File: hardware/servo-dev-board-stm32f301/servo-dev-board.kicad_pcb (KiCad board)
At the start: 4 copper layers, 51.5 x 26.5 mm, 39 parts, among them J1 USB_B_Micro, J2 Conn_01x05_MountingPin, J3 Conn_01x04_MountingPin, J4 Conn_01x04_MountingPin, J5 Conn_02x05_Odd_Even, SW1 SW_Push, SW2 SW_Push, U1 DRV8231ADSGR, U2 SSP7615-33DFR, U3 STM32F301K8Ux, Y1 16MHz 9pF

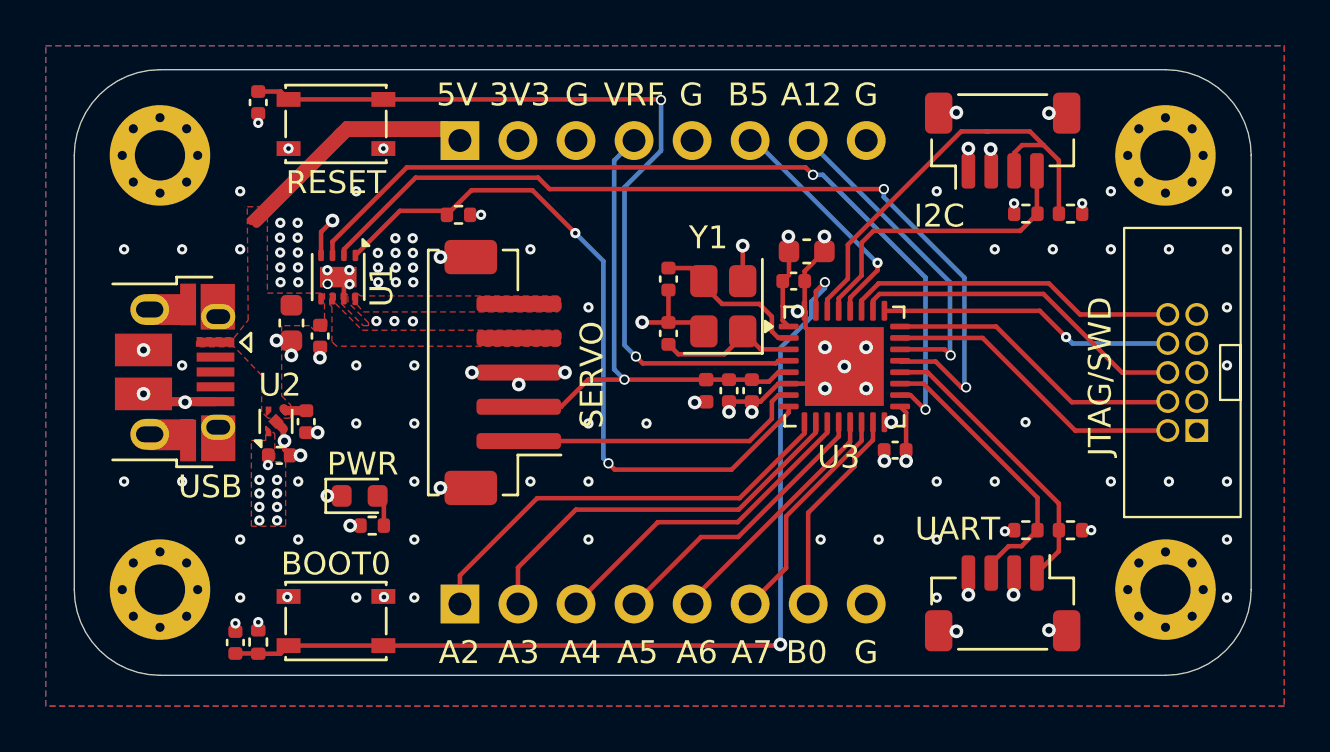
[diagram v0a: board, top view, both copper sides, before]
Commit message: update usb connector due to parts shortage
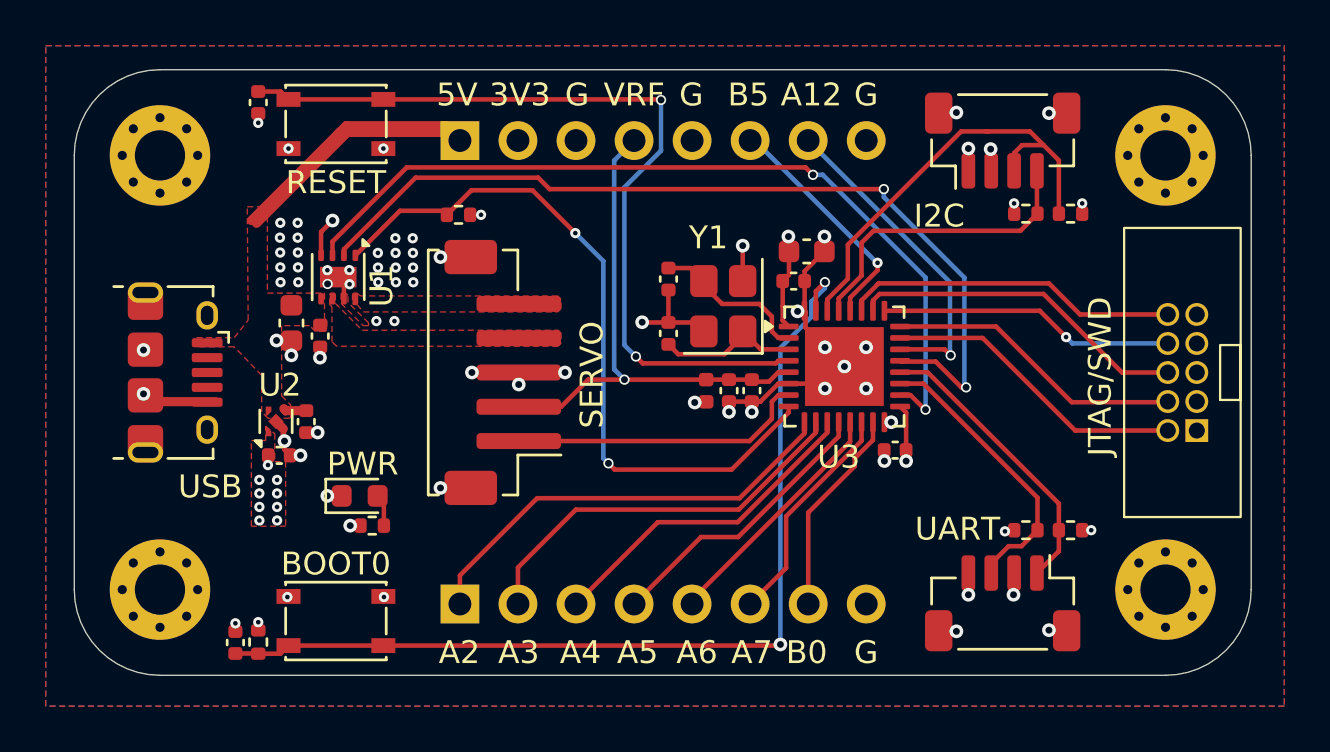
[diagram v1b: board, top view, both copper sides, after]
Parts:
- J1: footprint Connector_USB:USB_Micro-B_Amphenol_10103594-0001LF_Horizontal -> Connector_USB:USB_Micro-B_Amphenol_10118194-0001LF_Horizontal
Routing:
- net GND: vias 117 -> 66
